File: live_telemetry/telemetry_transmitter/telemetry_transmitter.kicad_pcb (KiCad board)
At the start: 2 copper layers, 50.8 x 61 mm, 62 parts, among them J1 Programming Header, J2 Battery In, J3 BUS_CONN, J4 Conn_Coaxial, Q1 Q_NMOS_GSD, Q2 Q_NMOS_GSD, Q3 Q_PMOS_GSD, Q4 Q_PMOS_GSD, Q5 Q_NMOS_GSD, U1 PIC18F26K83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

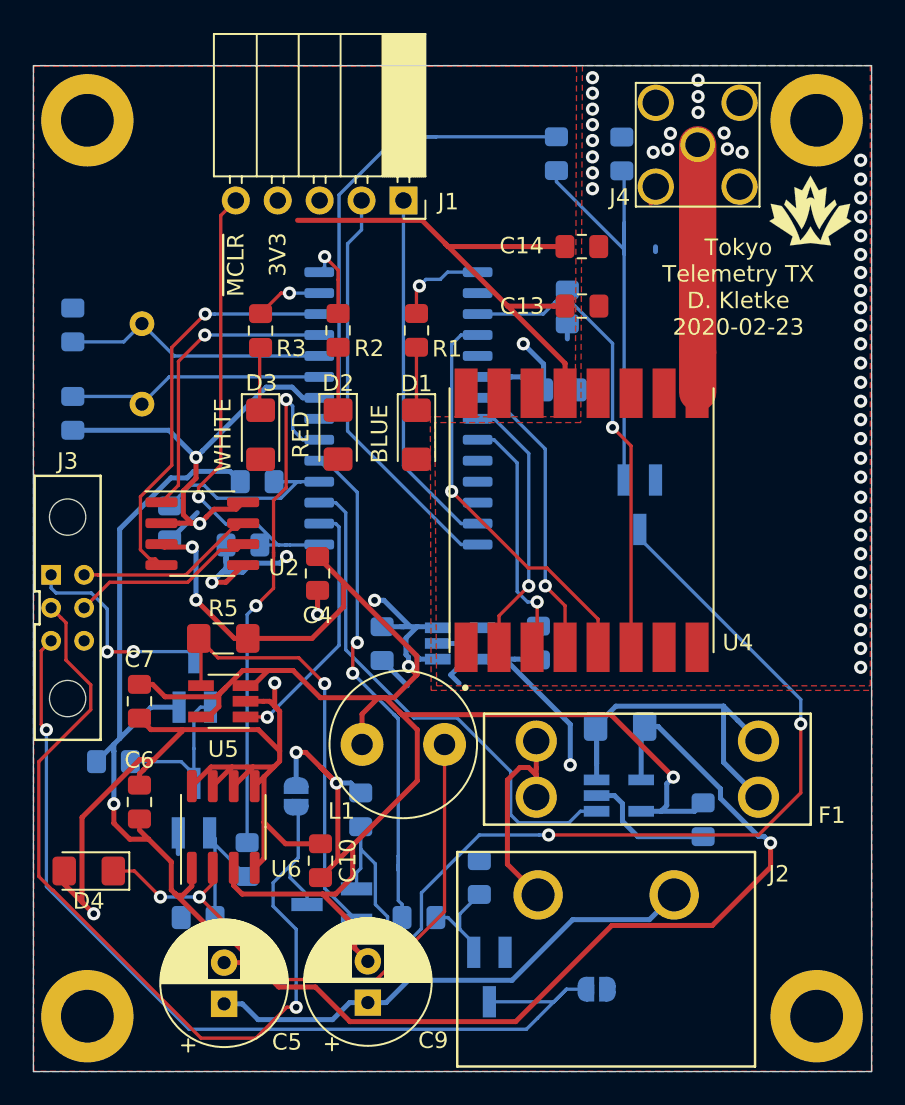
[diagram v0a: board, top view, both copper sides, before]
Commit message: Update schematics and silkscreens to fix issues from assembly
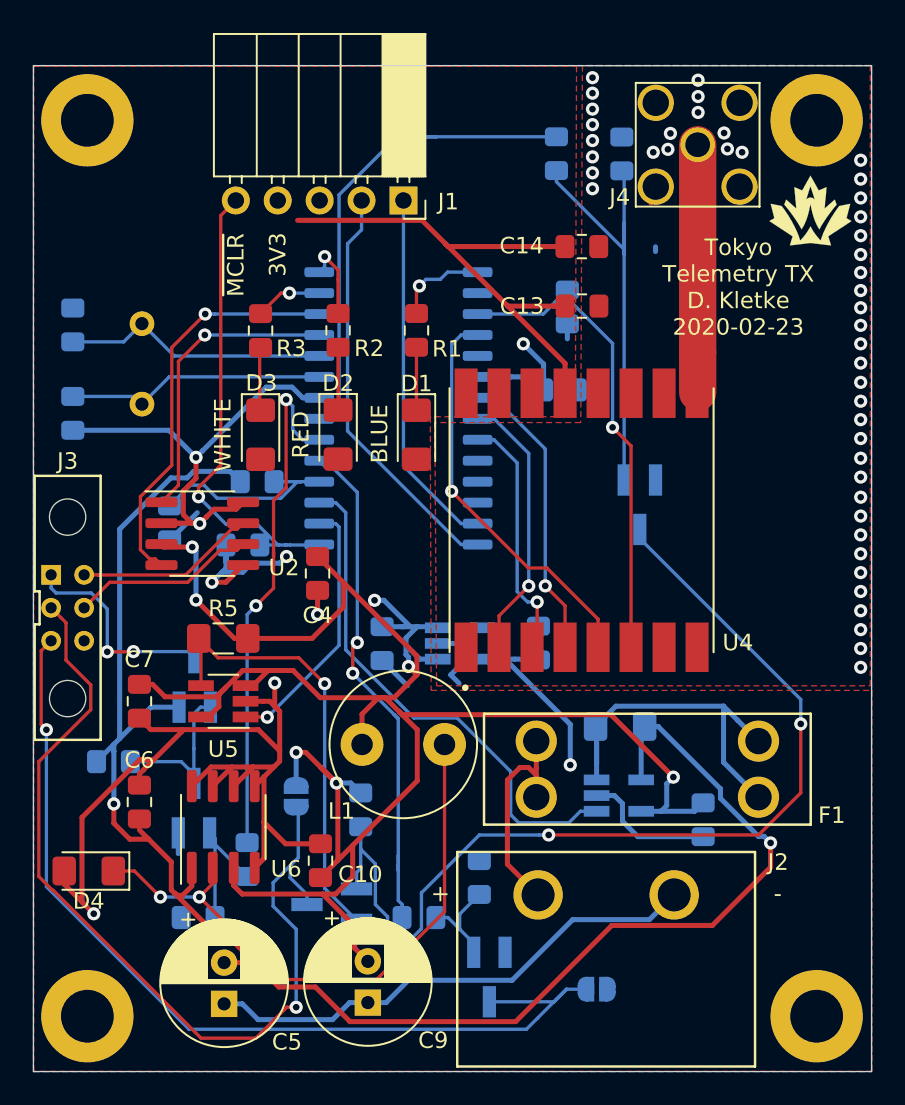
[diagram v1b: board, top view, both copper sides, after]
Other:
- board text added: "+"
- board text added: "-"
